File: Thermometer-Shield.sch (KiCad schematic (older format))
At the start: 47 parts, among them J1 Analog/I2C, J11 ShiftOut, J2 TempSensor, J3 Out-A, J4 Out-B, J5 Out-C, J6 Out-D, J7 Out-E, J8 Out-F, Q1 Q_PNP_BCE, Q2 Q_PNP_BCE, Q3 Q_PNP_BCE, Q4 Q_PNP_BCE, SW1 SW_SPST, SW2 SW_SPST, SW3 SW_SPST, SW4 SW_SPST, U1 74HC595, U2 74HC595, U3 ULN2803A

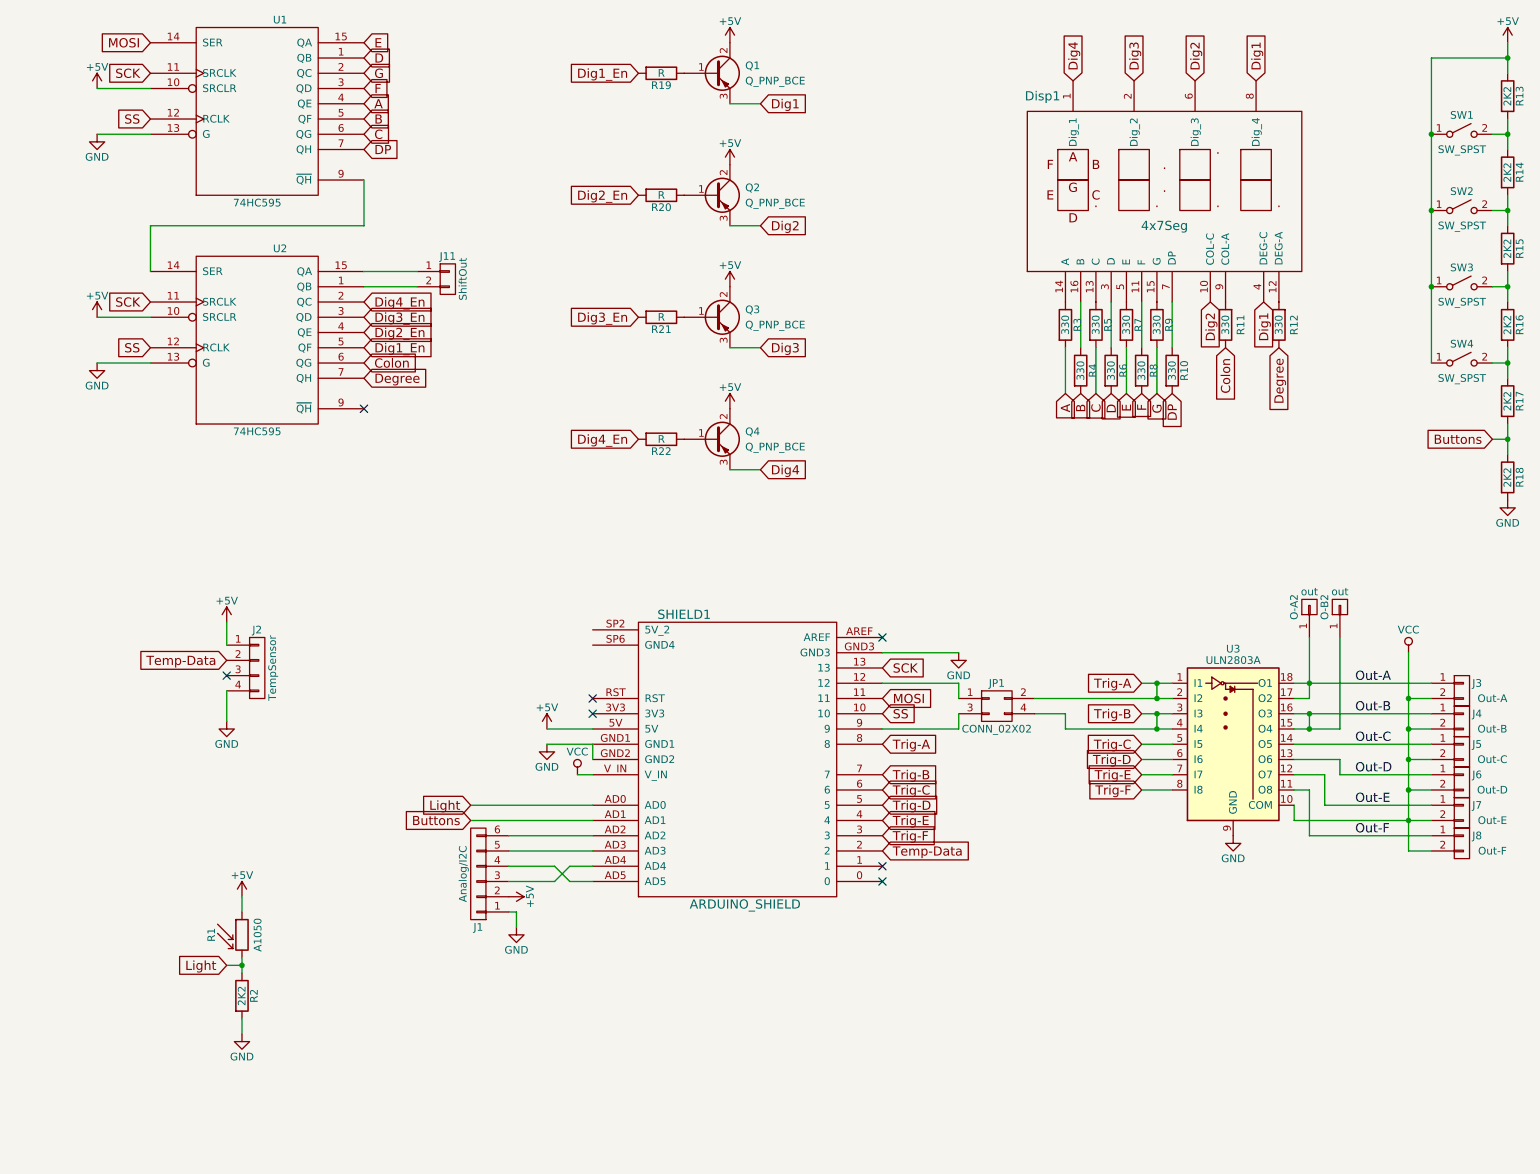
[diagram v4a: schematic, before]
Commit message: completed schematic and pcb
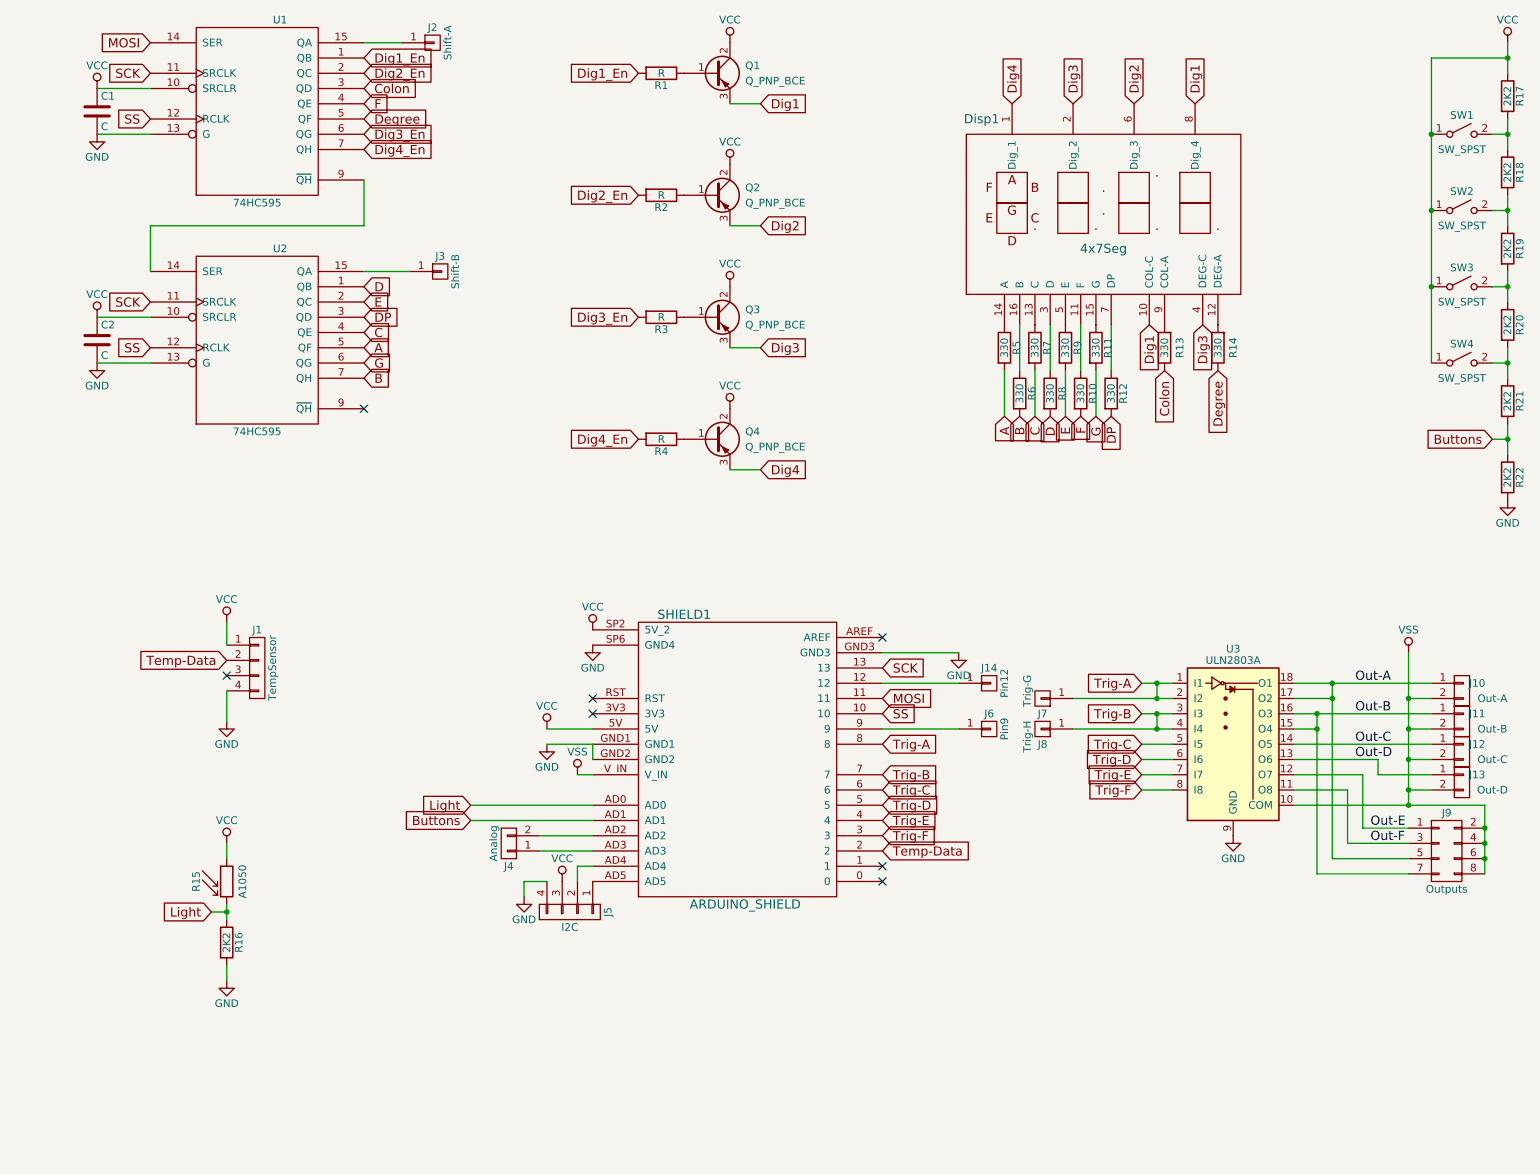
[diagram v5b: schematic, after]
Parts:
- removed J1: Analog/I2C, Pin_Headers:Pin_Header_Straight_1x06_Pitch2.54mm, symbol CONN_01X06
- removed J11: ShiftOut, Pin_Headers:Pin_Header_Straight_1x02_Pitch2.54mm, symbol CONN_01X02
- removed J7: Out-E, Connectors:AK300-2, symbol CONN_01X02
- removed J8: Out-F, Connectors:AK300-2, symbol CONN_01X02
- removed JP1: CONN_02X02, Pin_Headers:Pin_Header_Straight_2x02_Pitch2.54mm, symbol CONN_02X02
- removed O-A2, O-B2: out, Connectors:1pin, symbol CONN_01X01
- added C1, C2: C, Capacitors_THT:C_Disc_D5.0mm_W2.5mm_P5.00mm, symbol C
- added J14: Pin12, Pin_Headers:Pin_Header_Straight_1x01_Pitch2.54mm, symbol CONN_01X01
- added J2: Shift-A, Wire_Pads:SolderWirePad_single_0-8mmDrill, symbol CONN_01X01
- added J3: Shift-B, Wire_Pads:SolderWirePad_single_0-8mmDrill, symbol CONN_01X01
- added J4: Analog, Pin_Headers:Pin_Header_Straight_1x02_Pitch2.54mm, symbol CONN_01X02
- added J5: I2C, Pin_Headers:Pin_Header_Straight_1x04_Pitch2.54mm, symbol CONN_01X04
- added J6: Pin9, Pin_Headers:Pin_Header_Straight_1x01_Pitch2.54mm, symbol CONN_01X01
- added J7: Trig-G, Wire_Pads:SolderWirePad_single_0-8mmDrill, symbol CONN_01X01
- added J8: Trig-H, Wire_Pads:SolderWirePad_single_0-8mmDrill, symbol CONN_01X01
- added J9: Outputs, Pin_Headers:Pin_Header_Straight_2x04_Pitch2.54mm, symbol CONN_02X04
- Disp1: footprint Displays_7-Segment:AFF_2x7SEG-DIGIT_10mm -> SparkFun:ATA3492
- renumbered J2 to J1, J3 to J10, J4 to J11, J5 to J12, J6 to J13, R19 to R1, R8 to R10, R9 to R11, R10 to R12, R11 to R13, R12 to R14, R1 to R15, R2 to R16, R13 to R17, R14 to R18, R15 to R19, R20 to R2, R16 to R20, R17 to R21, R18 to R22, R21 to R3, R22 to R4, R3 to R5, R4 to R6, R5 to R7, R6 to R8, R7 to R9
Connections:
- net +5V is gone; now on net VCC: J1.1 (P1), Q1.2 (C), Q2.2 (C), Q3.2 (C), Q4.2 (C), R15.1, R17.1, SHIELD1.5V, SW1.1 (A), SW2.1 (A), SW3.1 (A), SW4.1 (A), U1.10 (SRCLR), U2.10 (SRCLR)
- net A: now also U2.5 (QF); no longer U1.4 (QE)
- net B: now also U2.7 (QH); no longer U1.5 (QF)
- net C: now also U2.4 (QE); no longer U1.6 (QG)
- net Colon: now also U1.3 (QD); no longer U2.6 (QG)
- net D: now also U2.1 (QB); no longer U1.1 (QB)
- net DP: now also U2.3 (QD); no longer U1.7 (QH)
- net Degree: now also U1.5 (QF); no longer U2.7 (QH)
- net Dig1: now also Disp1.10 (COL-C); no longer Disp1.4 (DEG-C)
- net Dig1_En: now also U1.1 (QB); no longer U2.5 (QF)
- net Dig2: no longer Disp1.10 (COL-C)
- net Dig2_En: now also U1.2 (QC); no longer U2.4 (QE)
- net Dig3: now also Disp1.4 (DEG-C)
- net Dig3_En: now also U1.6 (QG); no longer U2.3 (QD)
- net Dig4_En: now also U1.7 (QH); no longer U2.2 (QC)
- net E: now also U2.2 (QC); no longer U1.15 (QA)
- net F: now also U1.4 (QE); no longer U1.3 (QD)
- net G: now also U2.6 (QG); no longer U1.2 (QC)
- net GND: now also SHIELD1.SP6 (GND4), C1.2, C2.2, J5.4 (P4)
- net Out-A: now also J9.5 (P5)
- net Out-B: now also J9.7 (P7)
- net Out-E: now also J9.1 (P1)
- net Out-F: now also J9.3 (P3)
- net Trig-A: now also J7.1 (P1)
- net Trig-B: now also J8.1 (P1)
- net VCC: now also SHIELD1.SP2 (5V_2), C1.1, C2.1, J5.3 (P3); no longer J10.2 (P2), J11.2 (P2), J12.2 (P2), J13.2 (P2), SHIELD1.V_IN, U3.10 (COM)
- net at SHIELD1.12: now also J14.1 (P1)
- net at SHIELD1.9: now also J6.1 (P1)
- net at SHIELD1.AD2: now also J4.2 (P2)
- net at SHIELD1.AD3: now also J4.1 (P1)
- net at SHIELD1.AD4: now also J5.2 (P2)
- net at SHIELD1.AD5: now also J5.1 (P1)
- net at U2.15 (QA): now also J3.1 (P1)
- new net: J2.1 (P1), U1.15 (QA)
- new net VSS: J10.2 (P2), J11.2 (P2), J12.2 (P2), J13.2 (P2), J9.2 (P2), J9.4 (P4), J9.6 (P6), J9.8 (P8), SHIELD1.V_IN, U3.10 (COM)
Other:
- moved on the sheet: Disp1, R10, R11, R12, R13, R14, R15, R16, R5, R6, R7, R8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
